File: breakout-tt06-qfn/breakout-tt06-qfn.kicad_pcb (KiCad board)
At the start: 2 copper layers, 50 x 52 mm, 153 parts, among them J1 Conn_01x04, J10 U.FL, J11 U.FL, J12 U.FL, J13 U.FL, J2 U.FL, J3 U.FL, J4 U.FL, J5 U.FL, J6 U.FL, J7 U.FL, J8 U.FL, J9 U.FL, U1 Openframe_QFN_TT06_REV2, U2 24LC02

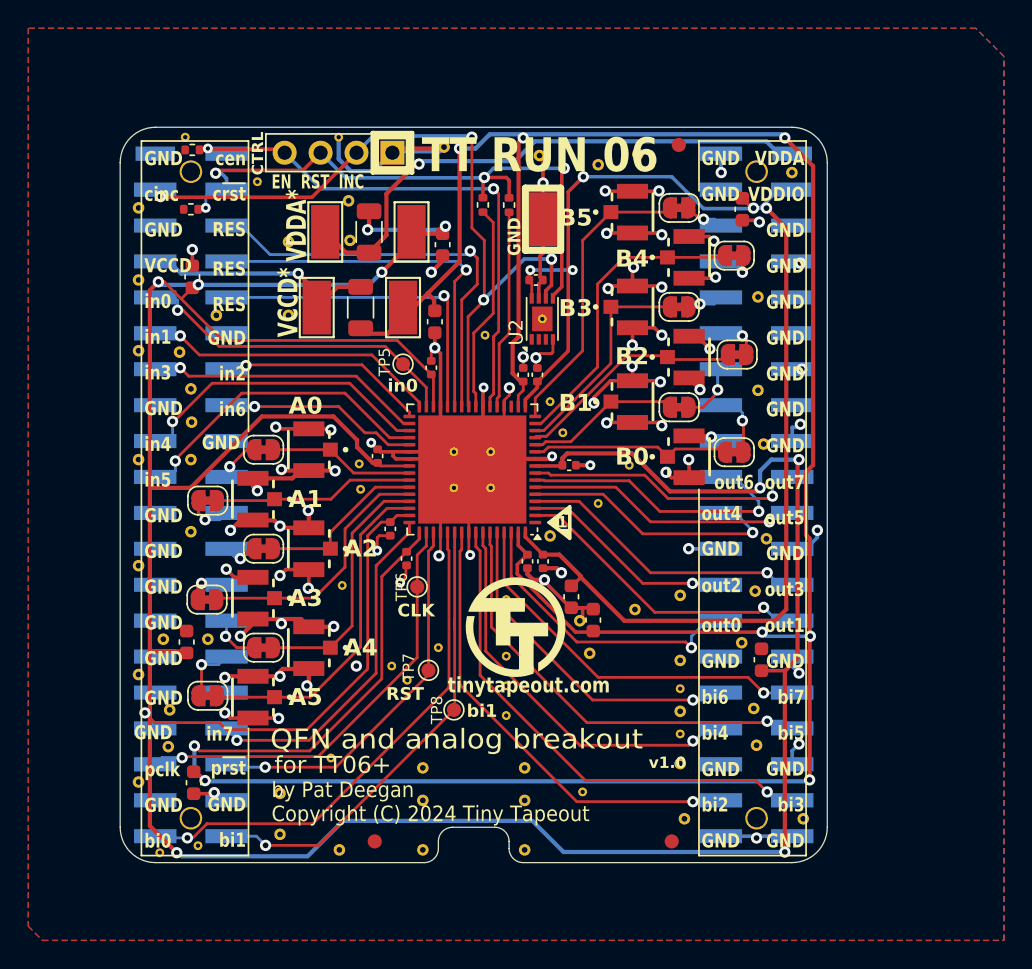
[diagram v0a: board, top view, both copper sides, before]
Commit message: CTRL MUX nReset and Increment lines crossed at chip: fixed
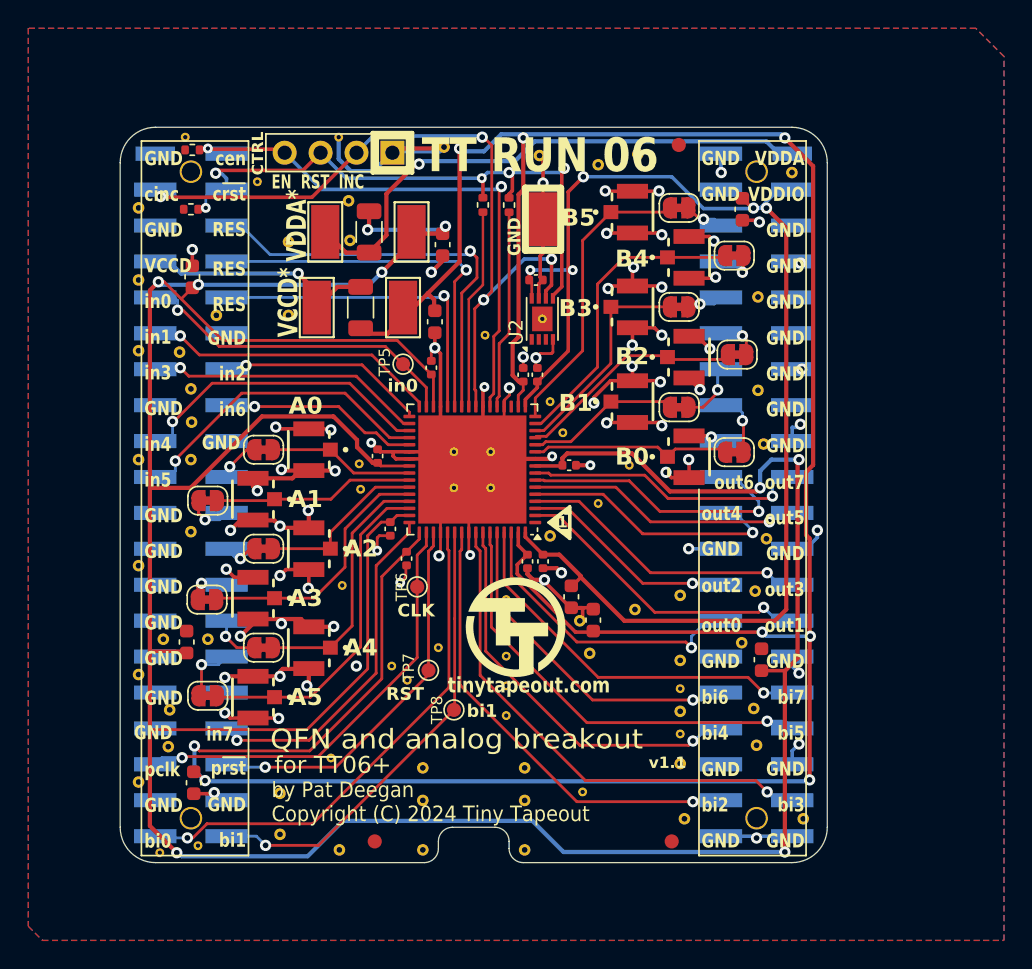
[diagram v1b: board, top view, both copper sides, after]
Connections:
- U1 pad 24: /c_rst_n -> /c_sel_inc
- U1 pad 25: /c_sel_inc -> /c_rst_n
- U2 pad 9: (no net) -> GND
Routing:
- net /hd_c_rst_n: track 45.1 -> 44.0 mm, vias 4 -> 5
- net /uio1: track 33.8 -> 33.0 mm
- net /c_sel_inc: track 53.4 -> 54.1 mm
- net /c_ena: track 38.4 -> 39.1 mm
- net /c_rst_n: track 14.7 -> 14.2 mm
- net vdda_all: vias 10 -> 9
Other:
- board text added: "v1.1"
- board text removed: "v1.0"
